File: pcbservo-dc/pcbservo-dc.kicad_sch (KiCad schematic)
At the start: 29 parts, among them J10 Conn_01x03, J12 Conn_01x02, J13 Conn_01x02, J4 Conn_01x03, J5 Conn_01x03, SW1 SW_Nidec_CAS-120A1, SW2 SW_Nidec_CAS-120A1, SW3 SW_Nidec_CAS-120A1, SW4 SW_Nidec_CAS-120A1, SW5 SW_Nidec_CAS-120A1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

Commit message: uart a jour
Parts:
- removed H3: MountingHole_Pad, MountingHole:MountingHole_2.7mm_M2.5_Pad, symbol Mechanical:MountingHole_Pad
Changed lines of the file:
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@@
-	(wire
-		(pts
-			(xy 185.42 45.72) (xy 190.5 45.72)
-		)
-		(stroke
-			(width 0)
-			(type default)
-		)
-	)
 	(wire
 		(pts
@@
 	)
 	(symbol
-		(lib_id "power:GND")
-		(at 190.5 45.72 0)
-		(unit 1)
-		(exclude_from_sim no)
-		(in_bom yes)
-		(on_board yes)
-		(dnp no)
-		(fields_autoplaced yes)
-		(property "Reference" "#PWR013"
-			(at 190.5 52.07 0)
-			(effects
-				(font
-					(size 1.27 1.27)
-				)
-				(hide yes)
-			)
-		)
-		(property "Value" "GND"
-			(at 190.5 50.8 0)
-			(effects
-				(font
-					(size 1.27 1.27)
-				)
-				(hide yes)
-			)
-		)
-		(property "Footprint" ""
-			(at 190.5 45.72 0)
-			(effects
-				(font
-					(size 1.27 1.27)
-				)
-				(hide yes)
-			)
-		)
-		(property "Datasheet" ""
-			(at 190.5 45.72 0)
-			(effects
-				(font
-					(size 1.27 1.27)
-				)
-				(hide yes)
-			)
-		)
-		(property "Description" "Power symbol creates a global label with name \"GND\" , ground"
-			(at 190.5 45.72 0)
-			(effects
-				(font
-					(size 1.27 1.27)
-				)
-				(hide yes)
-			)
-		)
-		(pin "1"
-		)
-		(instances
-			(project "pcbservo-dc"
-				(path "/be41f19f-3f75-42cb-bbbf-7251912cb437"
-					(reference "#PWR013")
-					(unit 1)
-				)
-			)
-		)
-	)
-	(symbol
 		(lib_id "power:+7.5V")
 		(at 128.27 133.35 0)
@@
 					(unit 1)
 				)
-			)
-		)
-	)
-	(symbol
-		(lib_name "MountingHole_Pad_2")
-		(lib_id "Mechanical:MountingHole_Pad")
-		(at 182.88 45.72 90)
-		(unit 1)
-		(exclude_from_sim yes)
-		(in_bom no)
-		(on_board yes)
-		(dnp no)
-		(fields_autoplaced yes)
-		(property "Reference" "H3"
-			(at 181.61 41.91 90)
-			(effects
-				(font
-					(size 1.27 1.27)
-				)
-			)
-		)
-		(property "Value" "MountingHole_Pad"
-			(at 182.8799 43.18 0)
-			(effects
-				(font
-					(size 1.27 1.27)
-				)
-				(justify left)
-				(hide yes)
-			)
-		)
-		(property "Footprint" "MountingHole:MountingHole_2.7mm_M2.5_Pad"
-			(at 182.88 45.72 0)
-			(effects
-				(font
-					(size 1.27 1.27)
-				)
-				(hide yes)
-			)
-		)
-		(property "Datasheet" "~"
-			(at 182.88 45.72 0)
-			(effects
-				(font
-					(size 1.27 1.27)
-				)
-				(hide yes)
-			)
-		)
-		(property "Description" "Mounting Hole with connection"
-			(at 182.88 45.72 0)
-			(effects
-				(font
-					(size 1.27 1.27)
-				)
-				(hide yes)
-			)
-		)
-		(pin "1"
-		)
-		(instances
-			(project "pcbservo-dc"
-				(path "/be41f19f-3f75-42cb-bbbf-7251912cb437"
-					(reference "H3")
-					(unit 1)
-				)

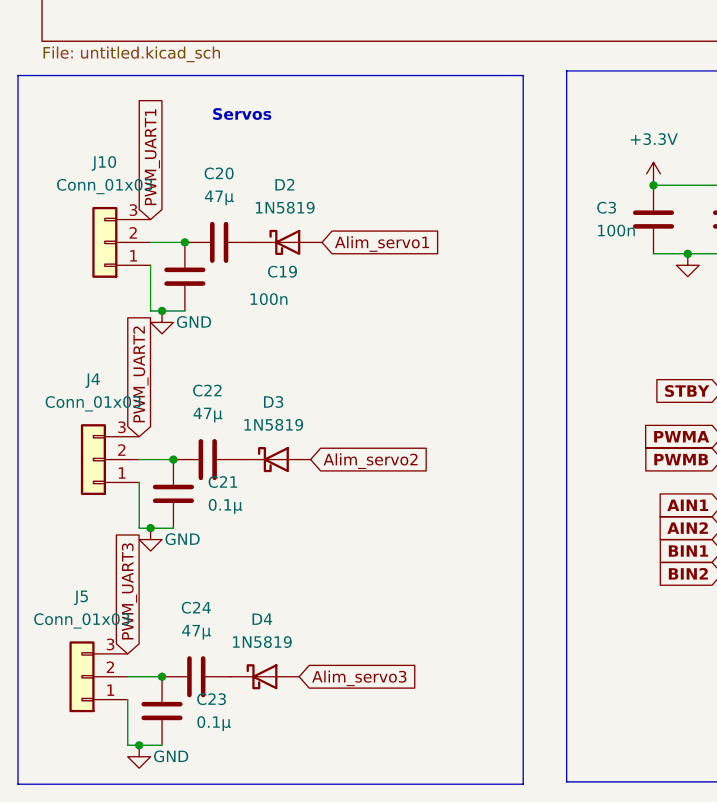
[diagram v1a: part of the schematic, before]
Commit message: modification des condensateur et des diode
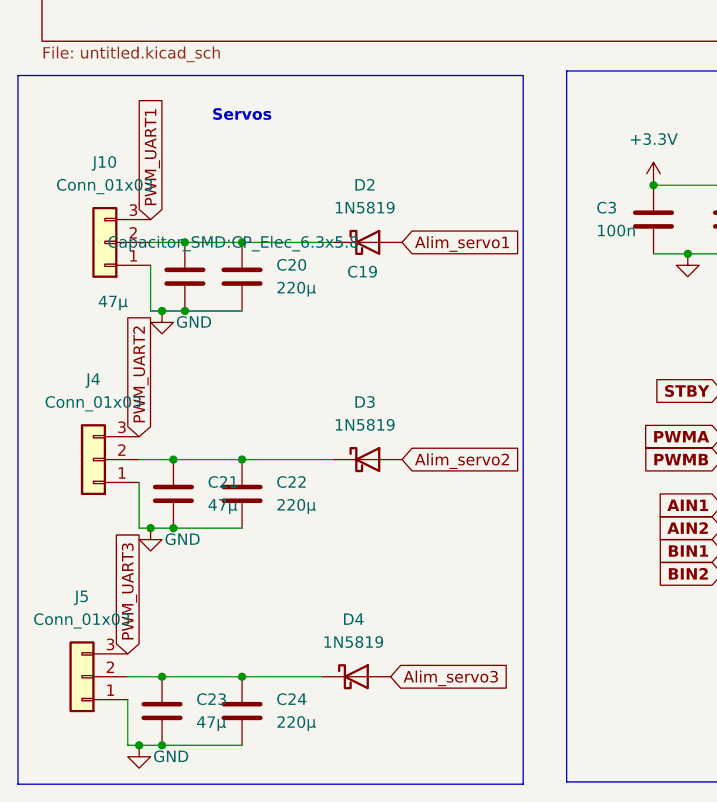
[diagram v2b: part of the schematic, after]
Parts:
- C19: value 100n -> 47µ; footprint Capacitor_SMD:C_0603_1608Metric -> Capacitor_SMD:C_0805_2012Metric
- C20, C22, C24: value 47µ -> 220µ; footprint Capacitor_SMD:CP_Elec_6.3x5.7 -> Capacitor_SMD:CP_Elec_6.3x5.8
- C21, C23: value 0.1µ -> 47µ; footprint Capacitor_SMD:C_0603_1608Metric -> Capacitor_SMD:C_0805_2012Metric
- D2, D3, D4: footprint Diode_THT:D_DO-41_SOD81_P10.16mm_Horizontal -> Diode_SMD:D_SOD-123
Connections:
- net GND: now also C20.1, C22.1, C24.1
- net at C21.1, J4.2 (Pin_2): now also C22.2, D3.1 (K); no longer C22.1
- net at C23.1, J5.2 (Pin_2): now also C24.2, D4.1 (K); no longer C24.1
- net at C19.1, J10.2 (Pin_2): now also C20.2, D2.1 (K); no longer C20.1
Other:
- moved on the sheet: C20, C22, C24, D2, D3, D4

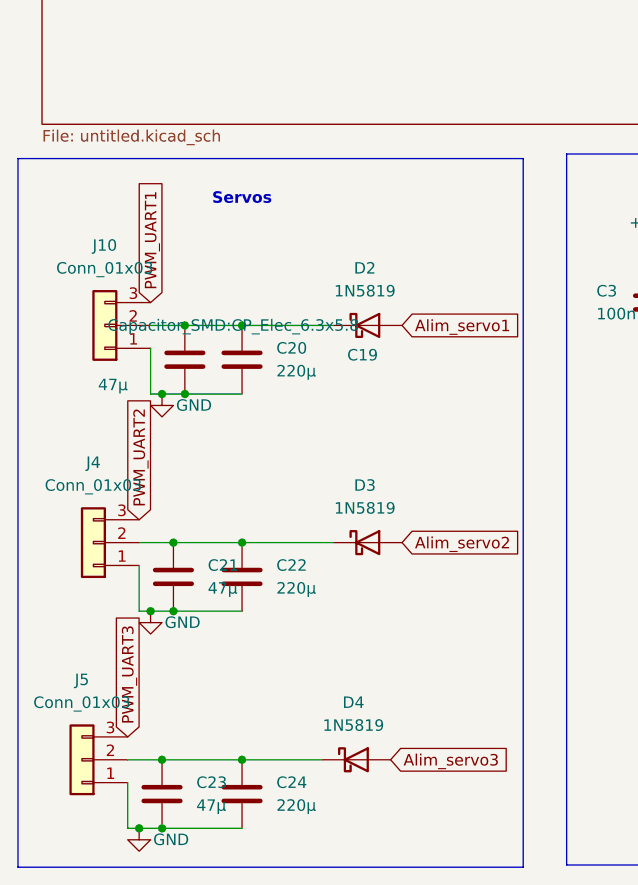
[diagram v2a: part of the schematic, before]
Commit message: changement de quelques empreinte
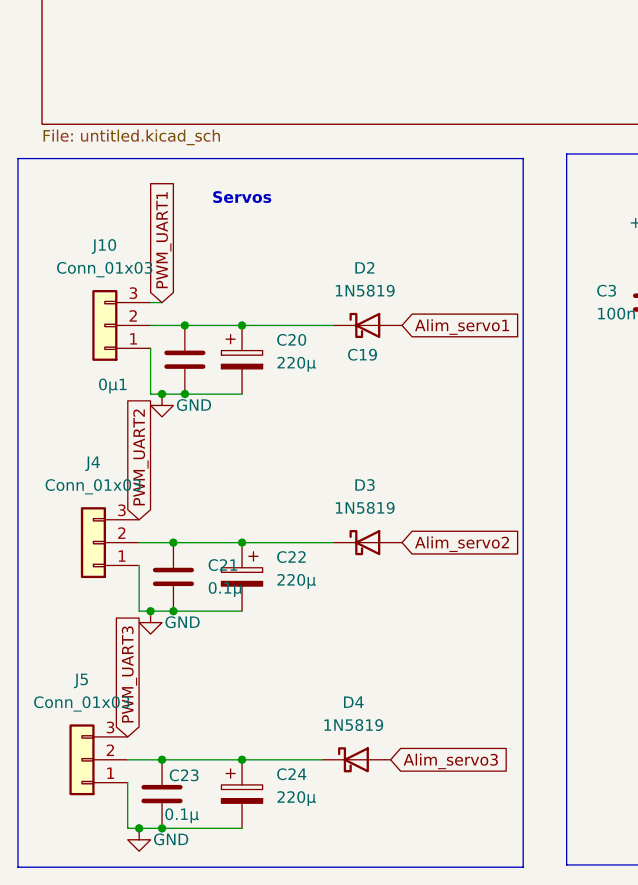
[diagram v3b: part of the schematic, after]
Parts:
- C19: value 47µ -> 0µ1
- C20, C22, C24: footprint Capacitor_SMD:CP_Elec_6.3x5.8 -> EEUFS1K221LB:CAPPRD500W60D1000H2500; symbol Device:C -> Device:C_Polarized
- C21, C23: value 47µ -> 0.1µ
- J10, J4, J5: footprint Connector_JST:JST_XH_B3B-XH-A_1x03_P2.50mm_Vertical -> Connector_JST:JST_EH_B3B-EH-A_1x03_P2.50mm_Vertical
- J12, J13: footprint Connector_JST:JST_XH_B2B-XH-A_1x02_P2.50mm_Vertical -> Connector_JST:JST_EH_B2B-EH-A_1x02_P2.50mm_Vertical
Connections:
- net GND: now also C20.2, C22.2, C24.2; no longer C20.1, C22.1, C24.1
- net at C21.1, D3.1 (K), J4.2 (Pin_2): now also C22.1; no longer C22.2
- net at C23.1, D4.1 (K), J5.2 (Pin_2): now also C24.1; no longer C24.2
- net at C19.1, D2.1 (K), J10.2 (Pin_2): now also C20.1; no longer C20.2
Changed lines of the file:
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@@
 	)
 	(junction
-		(at 38.1 137.16)
-		(diameter 0)
-		(color 0 0 0 0)
-	)
-	(junction
 		(at 118.11 133.35)
 		(diameter 0)
@@
 	)
 	(junction
-		(at 38.1 161.29)
+		(at 30.48 161.29)
 		(diameter 0)
 		(color 0 0 0 0)
 	)
 	(junction
-		(at 30.48 161.29)
+		(at 38.1 137.16)
 		(diameter 0)
 		(color 0 0 0 0)
@@
 	)
 	(junction
+		(at 38.1 161.29)
+		(diameter 0)
+		(color 0 0 0 0)
+	)
+	(junction
 		(at 114.3 133.35)
 		(diameter 0)
@@
 	(wire
 		(pts
-			(xy 38.1 161.29) (xy 48.26 161.29)
-		)
-		(stroke
-			(width 0)
-			(type default)
-		)
-	)
-	(wire
-		(pts
 			(xy 25.4 193.04) (xy 26.67 193.04)
 		)
@@
 	(wire
 		(pts
+			(xy 38.1 185.42) (xy 46.99 185.42)
+		)
+		(stroke
+			(width 0)
+			(type default)
+		)
+	)
+	(wire
+		(pts
 			(xy 118.11 133.35) (xy 128.27 133.35)
 		)
@@
 	(wire
 		(pts
+			(xy 38.1 137.16) (xy 48.26 137.16)
+		)
+		(stroke
+			(width 0)
+			(type default)
+		)
+	)
+	(wire
+		(pts
+			(xy 38.1 161.29) (xy 48.26 161.29)
+		)
+		(stroke
+			(width 0)
+			(type default)
+		)
+	)
+	(wire
+		(pts
 			(xy 109.22 189.23) (xy 109.22 190.5)
 		)
@@
 	(wire
 		(pts
-			(xy 38.1 185.42) (xy 46.99 185.42)
+			(xy 29.21 134.62) (xy 27.94 134.62)
 		)
 		(stroke
@@
 	(wire
 		(pts
-			(xy 38.1 137.16) (xy 48.26 137.16)
-		)
-		(stroke
-			(width 0)
-			(type default)
-		)
-	)
-	(wire
-		(pts
 			(xy 111.76 133.35) (xy 114.3 133.35)
 		)
@@
 	(global_label "PWM_UART1"
 		(shape input)
-		(at 27.94 134.62 90)
+		(at 29.21 134.62 90)
 		(fields_autoplaced yes)
 		(effects
@@
 		)
 		(property "Intersheetrefs" "${INTERSHEET_REFS}"
-			(at 27.94 120.6282 90)
+			(at 29.21 120.6282 90)
 			(effects
 				(font
@@
 			)
 		)
-		(property "Footprint" "Connector_JST:JST_XH_B3B-XH-A_1x03_P2.50mm_Vertical"
+		(property "Footprint" "Connector_JST:JST_EH_B3B-EH-A_1x03_P2.50mm_Vertical"
 			(at 21.59 161.29 0)
 			(effects
@@
 			)
 		)
-		(property "Footprint" "Connector_JST:JST_XH_B3B-XH-A_1x03_P2.50mm_Vertical"
+		(property "Footprint" "Connector_JST:JST_EH_B3B-EH-A_1x03_P2.50mm_Vertical"
 			(at 20.32 185.42 0)
 			(effects
@@
 		(on_board yes)
 		(dnp no)
-		(fields_autoplaced yes)
 		(property "Reference" "C23"
-			(at 33.02 187.9599 0)
+			(at 29.972 187.198 0)
 			(effects
 				(font
@@
 			)
 		)
-		(property "Value" "47µ"
-			(at 33.02 190.4999 0)
+		(property "Value" "0.1µ"
+			(at 29.464 191.516 0)
 			(effects
 				(font
@@
 			)
 		)
-		(property "Footprint" "Connector_JST:JST_XH_B3B-XH-A_1x03_P2.50mm_Vertical"
+		(property "Footprint" "Connector_JST:JST_EH_B3B-EH-A_1x03_P2.50mm_Vertical"
 			(at 22.86 137.16 0)
 			(effects
@@
 			)
 		)
-		(property "Footprint" "Connector_JST:JST_XH_B2B-XH-A_1x02_P2.50mm_Vertical"
+		(property "Footprint" "Connector_JST:JST_EH_B2B-EH-A_1x02_P2.50mm_Vertical"
 			(at 127 102.87 0)
 			(effects
@@
 	)
 	(symbol
-		(lib_id "Device:C")
-		(at 38.1 140.97 180)
+		(lib_id "Device:C_Polarized")
+		(at 38.1 140.97 0)
 		(unit 1)
 		(exclude_from_sim no)
@@
 		(fields_autoplaced yes)
 		(property "Reference" "C20"
-			(at 41.91 139.6999 0)
+			(at 41.91 138.8109 0)
 			(effects
 				(font
 					(size 1.27 1.27)
 				)
-				(justify right)
+				(justify left)
 			)
 		)
 		(property "Value" "220µ"
-			(at 41.91 142.2399 0)
+			(at 41.91 141.3509 0)
 			(effects
 				(font
 					(size 1.27 1.27)
 				)
-				(justify right)
+				(justify left)
 			)
 		)
-		(property "Footprint" "Capacitor_SMD:CP_Elec_6.3x5.8"
-			(at 37.1348 137.16 0)
+		(property "Footprint" "EEUFS1K221LB:CAPPRD500W60D1000H2500"
+			(at 39.0652 144.78 0)
 			(effects
 				(font
 					(size 1.27 1.27)
 				)
+				(hide yes)
 			)
 		)
@@
 			)
 		)
-		(property "Description" "Unpolarized capacitor"
+		(property "Description" "Polarized capacitor"
 			(at 38.1 140.97 0)
 			(effects
@@
 			)
 		)
-		(property "Footprint" "Connector_JST:JST_XH_B2B-XH-A_1x02_P2.50mm_Vertical"
+		(property "Footprint" "Connector_JST:JST_EH_B2B-EH-A_1x02_P2.50mm_Vertical"
 			(at 127 92.71 0)
 			(effects
@@
 	)
 	(symbol
-		(lib_id "Device:C")
-		(at 38.1 189.23 180)
+		(lib_id "Device:C_Polarized")
+		(at 38.1 189.23 0)
 		(unit 1)
 		(exclude_from_sim no)
@@
 		(fields_autoplaced yes)
 		(property "Reference" "C24"
-			(at 41.91 187.9599 0)
+			(at 41.91 187.0709 0)
 			(effects
 				(font
 					(size 1.27 1.27)
 				)
-				(justify right)
+				(justify left)
 			)
 		)
 		(property "Value" "220µ"
-			(at 41.91 190.4999 0)
+			(at 41.91 189.6109 0)
 			(effects
 				(font
 					(size 1.27 1.27)
 				)
-				(justify right)
+				(justify left)
 			)
 		)
-		(property "Footprint" "Capacitor_SMD:CP_Elec_6.3x5.8"
-			(at 37.1348 185.42 0)
+		(property "Footprint" "EEUFS1K221LB:CAPPRD500W60D1000H2500"
+			(at 39.0652 193.04 0)
 			(effects
 				(font
@@
 			)
 		)
-		(property "Description" "Unpolarized capacitor"
+		(property "Description" "Polarized capacitor"
 			(at 38.1 189.23 0)
 			(effects
@@
 			)
 		)
-		(property "Value" "47µ"
+		(property "Value" "0.1µ"
 			(at 34.29 166.3699 0)
 			(effects
@@
 	)
 	(symbol
-		(lib_id "Device:C")
-		(at 38.1 165.1 180)
+		(lib_id "Device:C_Polarized")
+		(at 38.1 165.1 0)
+		(mirror y)
 		(unit 1)
 		(exclude_from_sim no)
@@
 		(fields_autoplaced yes)
 		(property "Reference" "C22"
-			(at 41.91 163.8299 0)
+			(at 41.91 162.9409 0)
 			(effects
 				(font
@@
 		)
 		(property "Value" "220µ"
-			(at 41.91 166.3699 0)
+			(at 41.91 165.4809 0)
 			(effects
 				(font
@@
 			)
 		)
-		(property "Footprint" "Capacitor_SMD:CP_Elec_6.3x5.8"
-			(at 37.1348 161.29 0)
+		(property "Footprint" "EEUFS1K221LB:CAPPRD500W60D1000H2500"
+			(at 37.1348 168.91 0)
 			(effects
 				(font
@@
 			)
 		)
-		(property "Description" "Unpolarized capacitor"
+		(property "Description" "Polarized capacitor"
 			(at 38.1 165.1 0)
 			(effects
@@
 			)
 		)
-		(property "Value" "47µ"
+		(property "Value" "0µ1"
 			(at 22.098 143.764 0)
 			(effects
